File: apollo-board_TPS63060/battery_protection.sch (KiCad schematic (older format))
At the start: 11 parts, among them J1 JST_PH_S2B_thru, Q1 DMN2019UTS, U1 AP9101CK6-AYTRG1

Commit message: Remove unused parts at schematic level.
+ solve schematic DRC issues
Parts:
- removed BT1: Battery_Cell_Holder_18650_SMT_1042, Battery:BatteryHolder_Keystone_1042_1x18650, symbol battery_cell_holder_18650_smt_1042:Battery_Cell_Holder_18650_SMT_1042
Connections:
- wire segments 56 -> 52
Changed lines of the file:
@@
 $EndComp
-Wire Wire Line
-	3800 1500 3800 1400
-Wire Wire Line
-	3800 1800 3800 1900
 Wire Wire Line
 	3550 1700 3550 1900
@@
 Wire Wire Line
 	3550 1400 3800 1400
-Connection ~ 3800 1400
-Wire Wire Line
-	3800 1400 3800 1300
 Text Notes 8150 2450 0    50   ~ 0
 Chinese Chip price range from LCSC (10/2020) :\n$0.075-0.115 @qt=10\n$0.054-0.087 @qt=100
@@
 Wire Wire Line
 	3550 1700 3200 1700
-Connection ~ 3800 1900
 Text Notes 2100 1300 0    50   ~ 0
 External Battery connector
@@
 Text Notes 1400 3600 0    50   ~ 0
 +12Vmax
-$Comp
-L battery_cell_holder_18650_smt_1042:Battery_Cell_Holder_18650_SMT_1042 BT1
-U 1 1 5FD97812
-P 3800 1700
-F 0 "BT1" H 3918 1841 50  0000 L CNN
-F 1 "Battery_Cell_Holder_18650_SMT_1042" H 3900 1700 50  0001 L CNN
-F 2 "Battery:BatteryHolder_Keystone_1042_1x18650" V 3800 1760 50  0001 C CNN
-F 3 "https://www.keyelco.com/product-pdf.cfm?p=918" V 3800 1760 50  0001 C CNN
-F 4 "Keystone" H 3918 1750 50  0000 L CNN "Mfr_name"
-F 5 "1042" H 3918 1659 50  0000 L CNN "Mfr_no"
-F 6 "https://octopart.com/1042-keystone-19977746?r=sp#PriceAndStock" H 3800 1700 50  0001 C CNN "Octopart_link"
-F 7 "https://fr.farnell.com/keystone/1042p/battery-holder-18650-smd/dp/2674338?ost=keystone+1042" H 3800 1700 50  0001 C CNN "Farnell_link"
-F 8 "?" H 3800 1700 50  0001 C CNN "Farnell_ref"
-F 9 "2020-11-29" H 3800 1700 50  0001 C CNN "Farnell_check_date"
-F 10 "2,94 €" H 3800 1700 50  0001 C CNN "Farnell_price_qt=1"
-F 11 "2,65 €" H 3800 1700 50  0001 C CNN "Farnell_price_qt=10"
-F 12 "2,26 €" H 3800 1700 50  0001 C CNN "Farnell_price_qt=100"
-F 13 "1,62 €" H 3800 1700 50  0001 C CNN "Farnell_price_qt=1000"
-F 14 "Available from 2021-01-16" H 3800 1700 50  0001 C CNN "Farnell_stock"
-F 15 "-" H 3800 1700 50  0001 C CNN "LCSC_link"
-F 16 "-" H 3800 1700 50  0001 C CNN "LCSC_ref"
-F 17 "2020-11-29" H 3800 1700 50  0001 C CNN "LCSC_check_date"
-F 18 "-" H 3800 1700 50  0001 C CNN "LCSC_price_qt=1"
-F 19 "-" H 3800 1700 50  0001 C CNN "LCSC_price_qt=10"
-F 20 "-" H 3800 1700 50  0001 C CNN "LCSC_price_qt=100"
-F 21 "-" H 3800 1700 50  0001 C CNN "LCSC_price_qt=1000"
-F 22 "-" H 3800 1700 50  0001 C CNN "LCSC_stock"
-F 23 "https://eu.mouser.com/ProductDetail/Keystone-Electronics/1042?qs=%2F7TOpeL5Mz4qPdWi9tuLKw%3D%3D" H 3800 1700 50  0001 C CNN "Mouser_link"
-F 24 "?" H 3800 1700 50  0001 C CNN "Mouser_ref"
-F 25 "2020-11-29" H 3800 1700 50  0001 C CNN "Mouser_check_date"
-F 26 "$3.62" H 3800 1700 50  0001 C CNN "Mouser_price_qt=1"
-F 27 "-" H 3800 1700 50  0001 C CNN "Mouser_price_qt=10"
-F 28 "$3.13" H 3800 1700 50  0001 C CNN "Mouser_price_qt=100"
-F 29 "$2.36" H 3800 1700 50  0001 C CNN "Mouser_price_qt=1000"
-F 30 "3,942" H 3800 1700 50  0001 C CNN "Mouser_stock"
-F 31 "-" H 3800 1700 50  0001 C CNN "RS_link"
-F 32 "-" H 3800 1700 50  0001 C CNN "RS_ref"
-F 33 "2020-11-29" H 3800 1700 50  0001 C CNN "RS_check_date"
-F 34 "-" H 3800 1700 50  0001 C CNN "RS_price_qt=1"
-F 35 "-" H 3800 1700 50  0001 C CNN "RS_price_qt=10"
-F 36 "-" H 3800 1700 50  0001 C CNN "RS_price_qt=100"
-F 37 "-" H 3800 1700 50  0001 C CNN "RS_price_qt=1000"
-F 38 "-" H 3800 1700 50  0001 C CNN "RS_stock"
-F 39 "TO_CHECK" H 3800 1700 50  0001 C CNN "Status"
-F 40 "1.01" H 3800 1700 50  0001 C CNN "Release_version"
-F 41 "2020-12-12" H 3800 1700 50  0001 C CNN "Release_date"
-F 42 "ManWithNoName" H 3800 1700 50  0001 C CNN "Designer"
-	1    3800 1700
-	1    0    0    -1
-$EndComp
 Text Notes 3150 6550 0    50   ~ 0
 Do Not Populate (Default)
@@
 	-1   0    0    -1
 $EndComp
-Text Label 3550 1300 0    50   ~ 0
+Text Label 3800 1400 2    50   ~ 0
 VBAT
-Wire Wire Line
-	3550 1300 3800 1300
 Text Label 1700 3200 0    50   ~ 0
 VBAT

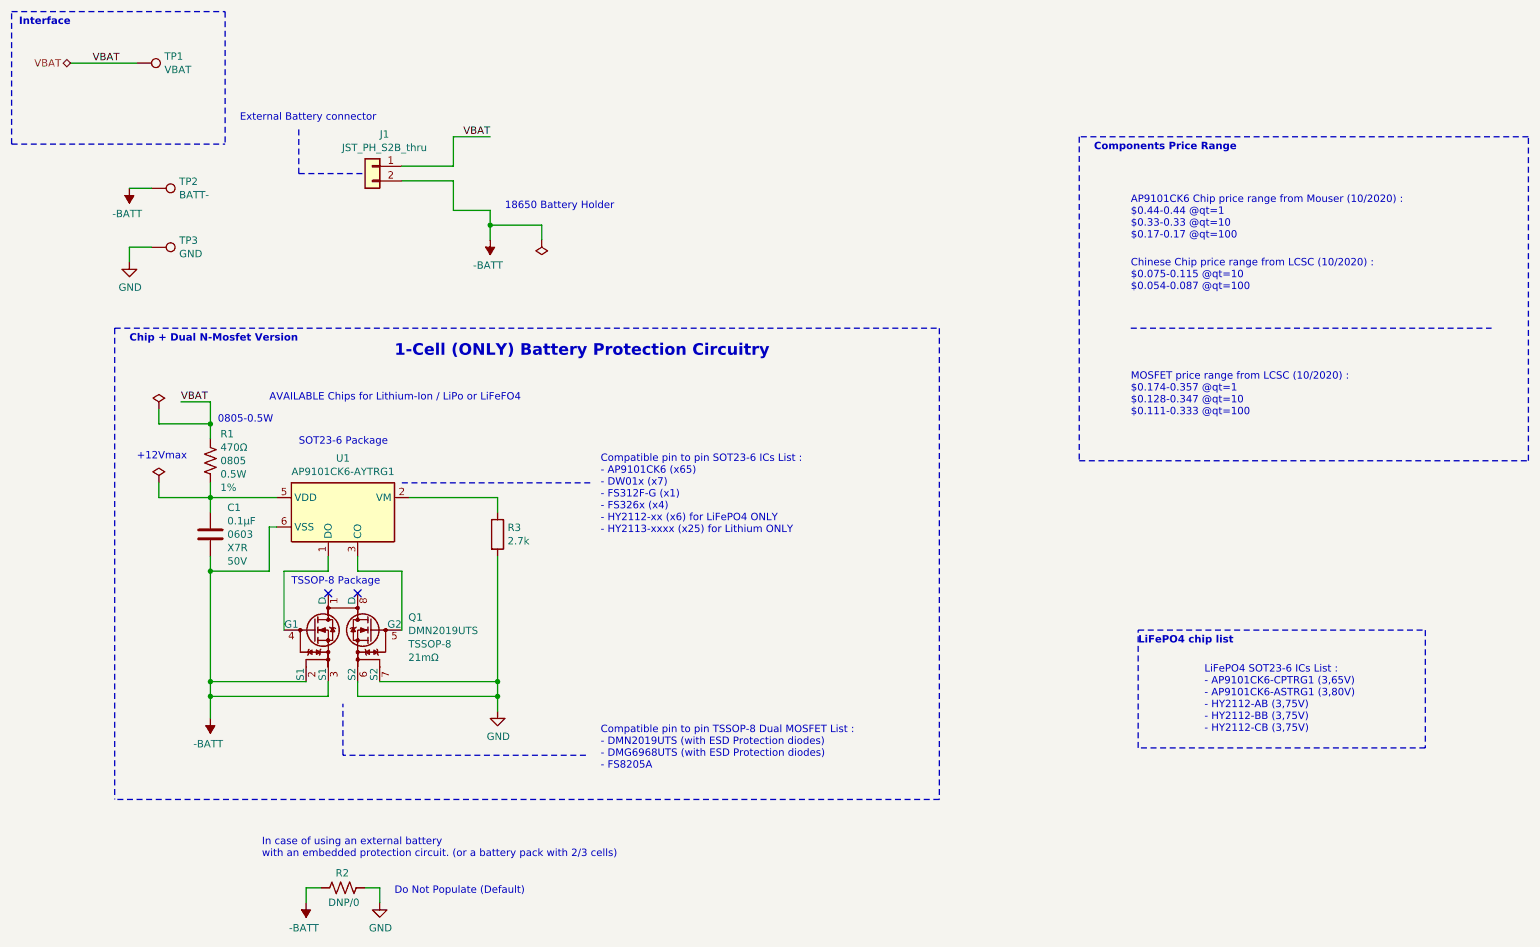
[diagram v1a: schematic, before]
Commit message: Add a Solder Jumper (shorted by default) between Vbat+ and R1 (AP9101)
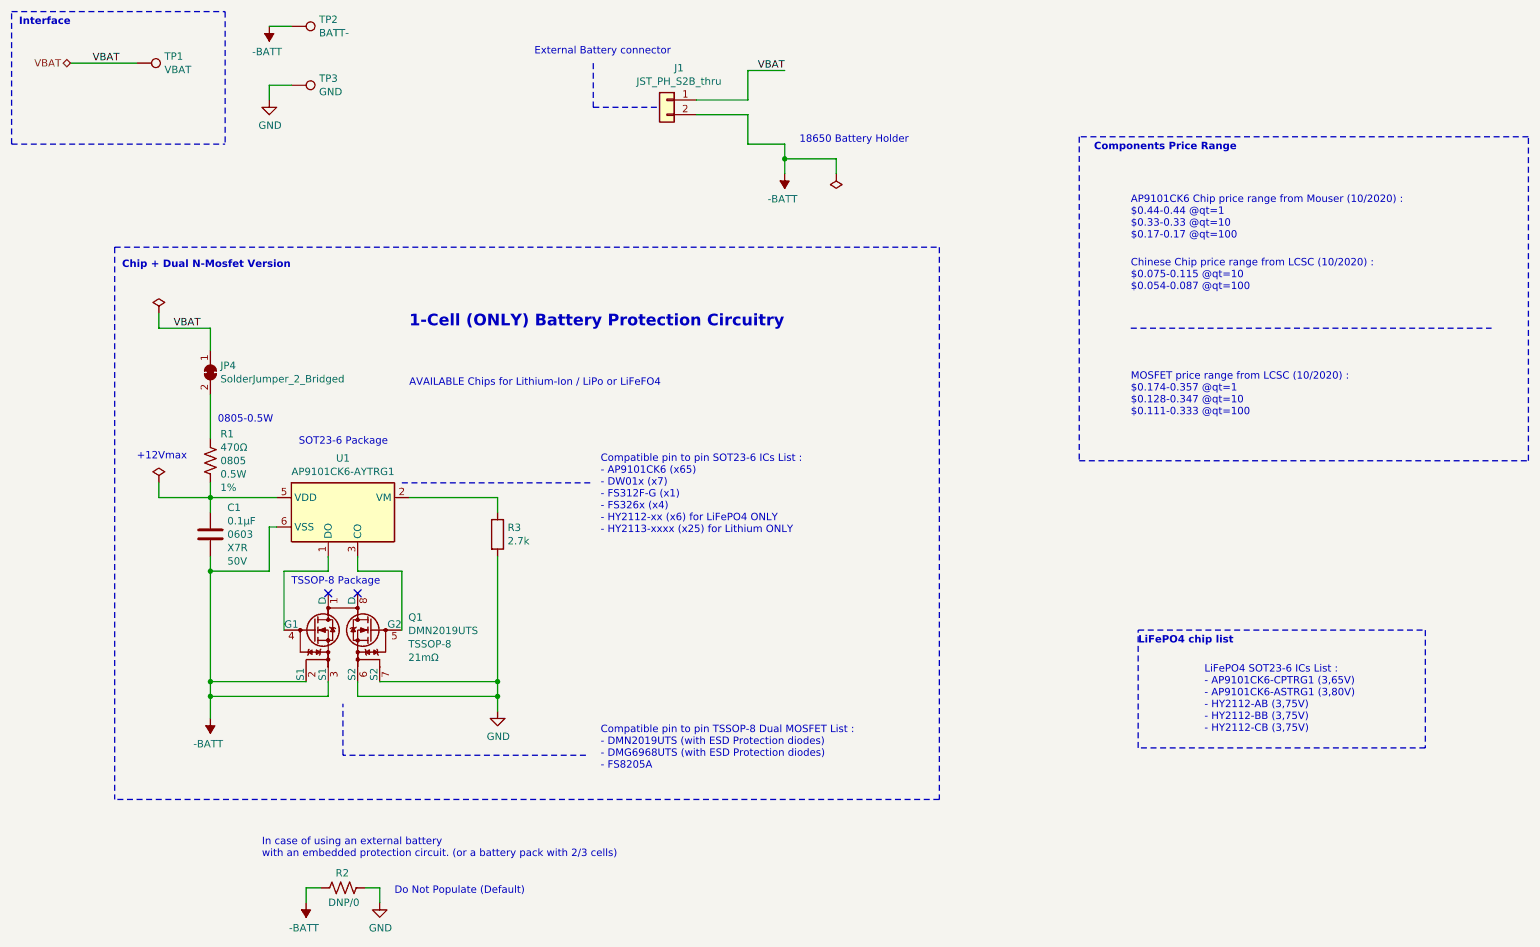
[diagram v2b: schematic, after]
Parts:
- added JP4: SolderJumper_2_Bridged, Jumper:SolderJumper-2_P1.3mm_Bridged_RoundedPad1.0x1.5mm, symbol Jumper:SolderJumper_2_Bridged
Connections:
- net VBAT: now also JP4.1 (A); no longer R1.1
- new net: JP4.2 (B), R1.1
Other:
- moved on the sheet: J1, TP2, TP3

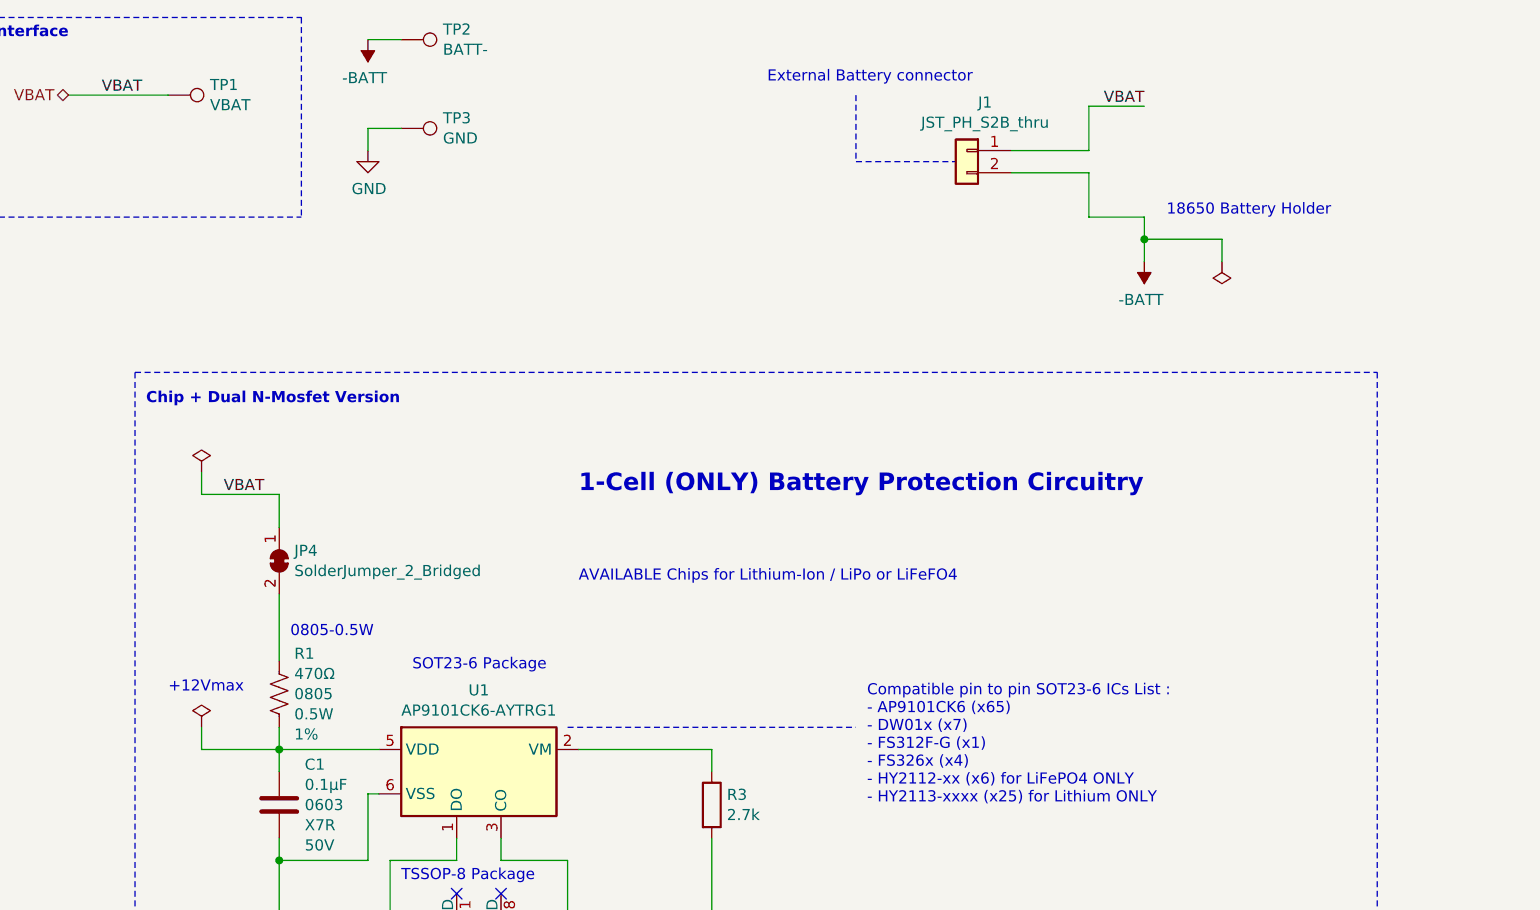
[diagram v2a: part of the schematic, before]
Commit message: Clean "Battery Protection IC" schematic
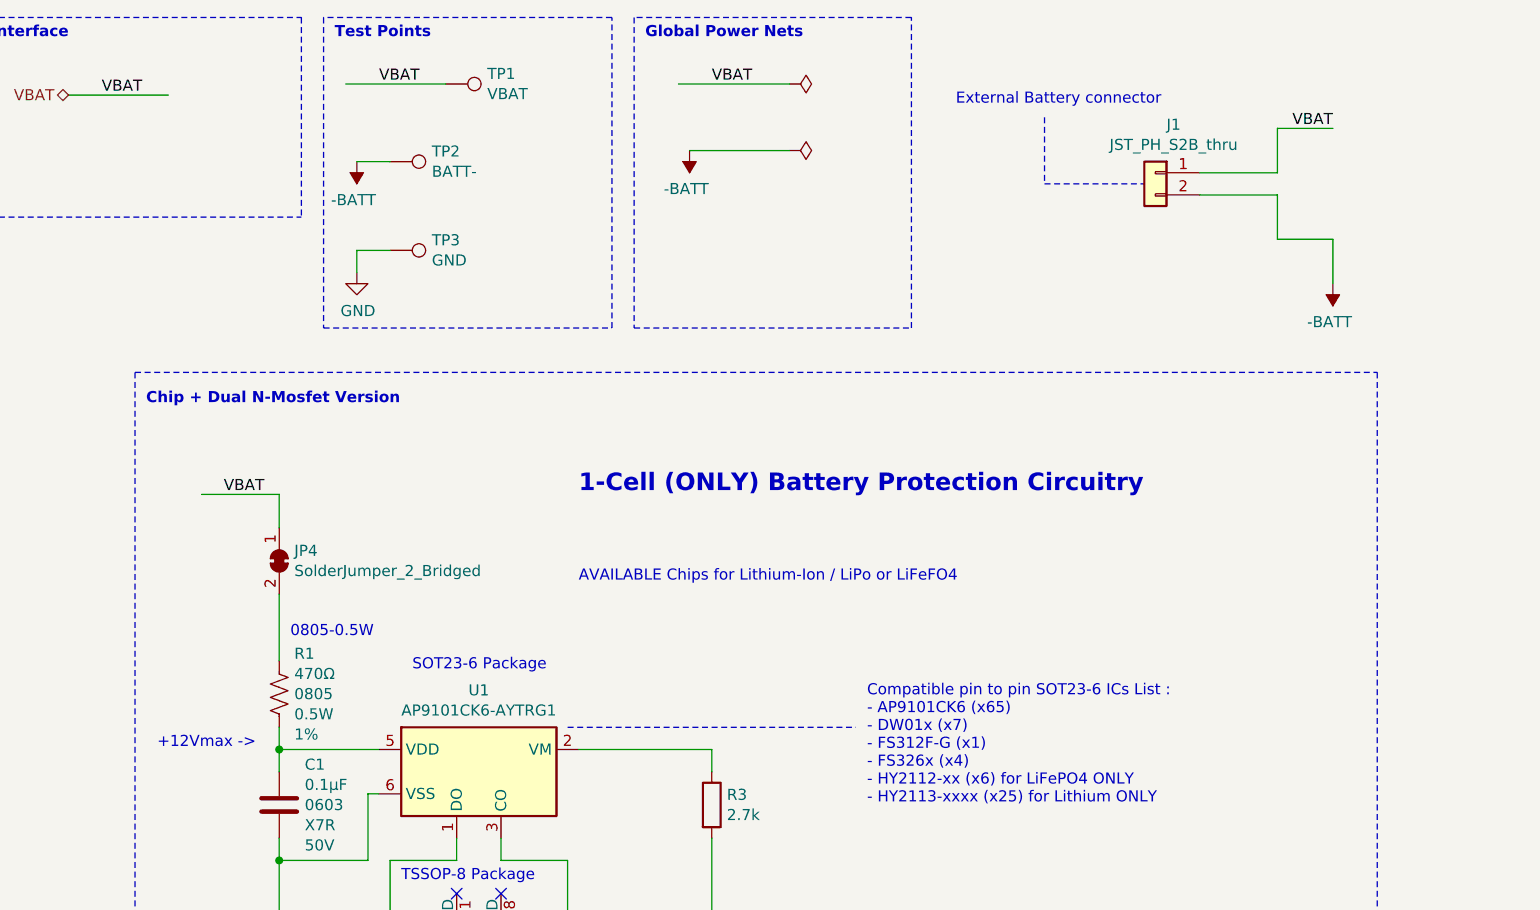
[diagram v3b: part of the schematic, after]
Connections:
- wire segments 51 -> 48
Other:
- note added: "+12Vmax ->"
- note added: "Global Power Nets"
- note added: "Test Points"
- note removed: "+12Vmax"
- note removed: "18650 Battery Holder"
- moved on the sheet: J1, TP1, TP2, TP3

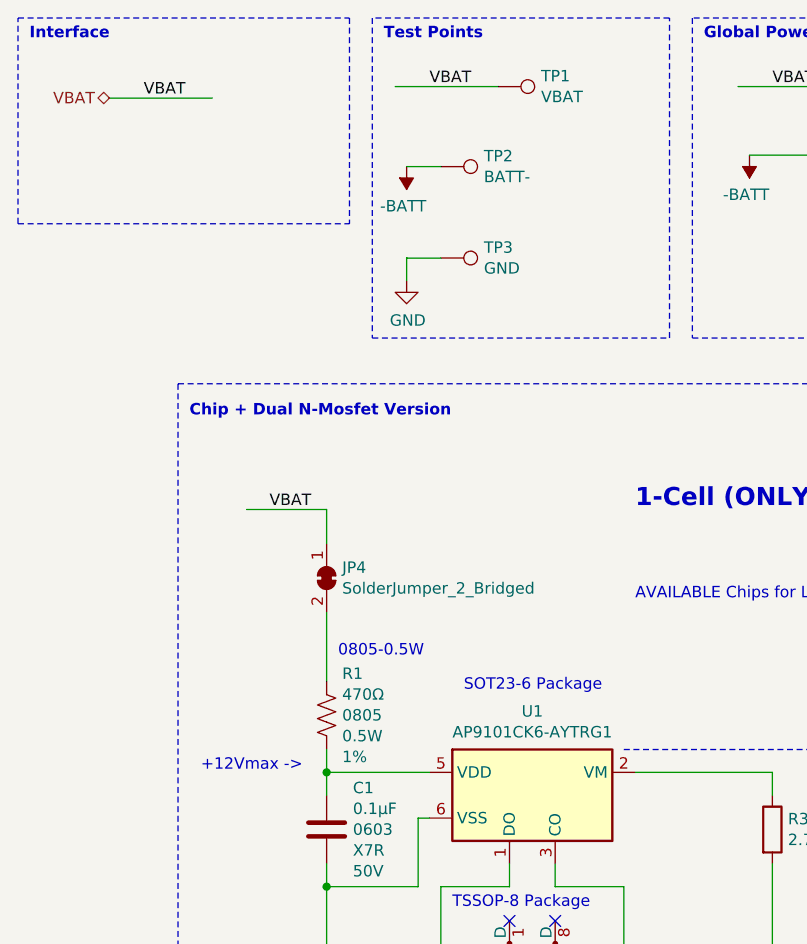
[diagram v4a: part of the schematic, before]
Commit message: Rename some power signal on Schematic to improve readability.
+ Misc. updates
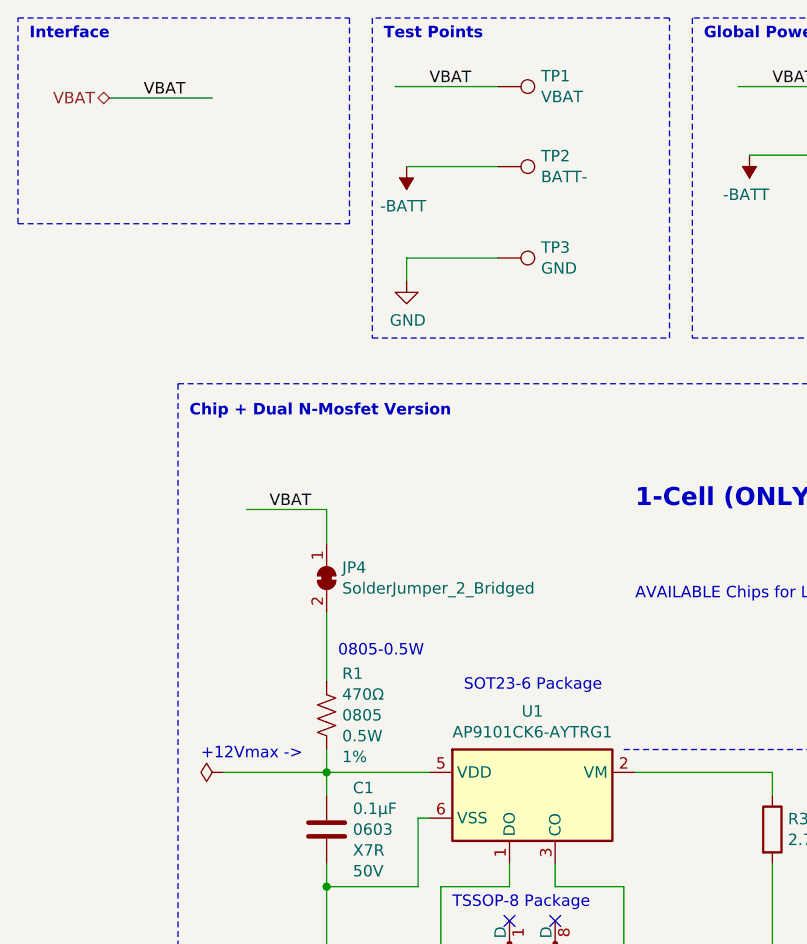
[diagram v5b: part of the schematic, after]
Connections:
- wire segments 48 -> 49
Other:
- moved on the sheet: TP2, TP3
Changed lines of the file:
@@
 L Connector:TestPoint TP2
 U 1 1 5FD99F7F
-P 2400 1200
-F 0 "TP2" V 2354 1388 50  0000 L CNN
-F 1 "BATT-" V 2445 1388 50  0000 L CNN
-F 2 "TestPoint:TestPoint_Pad_D1.0mm" H 2600 1200 50  0001 C CNN
-F 3 "~" H 2600 1200 50  0001 C CNN
-	1    2400 1200
+P 2650 1200
+F 0 "TP2" V 2604 1388 50  0000 L CNN
+F 1 "BATT-" V 2695 1388 50  0000 L CNN
+F 2 "TestPoint:TestPoint_Pad_D1.0mm" H 2850 1200 50  0001 C CNN
+F 3 "~" H 2850 1200 50  0001 C CNN
+	1    2650 1200
 	0    1    1    0
 $EndComp
@@
 $EndComp
 Wire Wire Line
-	2400 1200 2250 1200
+	2650 1200 2250 1200
 $Comp
 L Connector:TestPoint TP3
 U 1 1 5FDA33F6
-P 2400 1600
-F 0 "TP3" V 2354 1788 50  0000 L CNN
-F 1 "GND" V 2445 1788 50  0000 L CNN
-F 2 "TestPoint:TestPoint_Pad_D1.0mm" H 2600 1600 50  0001 C CNN
-F 3 "~" H 2600 1600 50  0001 C CNN
-	1    2400 1600
+P 2650 1600
+F 0 "TP3" V 2604 1788 50  0000 L CNN
+F 1 "GND" V 2695 1788 50  0000 L CNN
+F 2 "TestPoint:TestPoint_Pad_D1.0mm" H 2850 1600 50  0001 C CNN
+F 3 "~" H 2850 1600 50  0001 C CNN
+	1    2650 1600
 	0    1    1    0
 $EndComp
@@
 $EndComp
 Wire Wire Line
-	2400 1600 2250 1600
+	2650 1600 2250 1600
 Wire Wire Line
 	2250 1600 2250 1700
@@
 Text Notes 3250 2700 0    79   ~ 16
 1-Cell (ONLY) Battery Protection Circuitry
-Text Notes 1350 3850 0    50   ~ 0
+Text Notes 1350 3800 0    50   ~ 0
 +12Vmax ->
 Text Notes 3150 6550 0    50   ~ 0
@@
 	0    1    1    0
 $EndComp
+Wire Wire Line
+	1450 3850 1900 3850
+$Comp
+L power:PWR_FLAG #FLG0108
+U 1 1 610EB30B
+P 1450 3850
+F 0 "#FLG0108" H 1450 3925 50  0001 C CNN
+F 1 "PWR_FLAG" H 1450 4023 50  0001 C CNN
+F 2 "" H 1450 3850 50  0001 C CNN
+F 3 "~" H 1450 3850 50  0001 C CNN
+	1    1450 3850
+	0    -1   -1   0
+$EndComp
 $EndSCHEMATC
